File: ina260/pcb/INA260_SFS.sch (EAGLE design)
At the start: 52 parts

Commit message: finshed first design. after review ready for order
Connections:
- net SCL: now also BUS.P$1; no longer BUS.P$2
- net SDA: now also BUS.P$2; no longer BUS.P$1
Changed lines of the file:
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@@
 </busses>
 <nets>
-<net name="SCL" class="0">
-<segment>
-<pinref part="BUS" gate="J$1" pin="P$2"/>
-<wire x1="0" y1="8.89" x2="-10.16" y2="8.89" width="0.1524" layer="91"/>
-<label x="-10.16" y="6.35" size="1.778" layer="95"/>
-</segment>
-</net>
-<net name="SDA" class="0">
-<segment>
-<pinref part="BUS" gate="J$1" pin="P$1"/>
-<wire x1="0" y1="11.43" x2="-10.16" y2="11.43" width="0.1524" layer="91"/>
-<label x="-10.16" y="11.43" size="1.778" layer="95"/>
-</segment>
-</net>
 <net name="GND" class="0">
 <segment>
@@
 </segment>
 </net>
+<net name="SCL" class="0">
+<segment>
+<pinref part="BUS" gate="J$1" pin="P$1"/>
+<wire x1="0" y1="11.43" x2="-10.16" y2="11.43" width="0.1524" layer="91"/>
+<label x="-10.16" y="11.43" size="1.778" layer="95"/>
+</segment>
+</net>
+<net name="SDA" class="0">
+<segment>
+<pinref part="BUS" gate="J$1" pin="P$2"/>
+<wire x1="0" y1="8.89" x2="-10.16" y2="8.89" width="0.1524" layer="91"/>
+<label x="-10.16" y="6.35" size="1.778" layer="95"/>
+</segment>
+</net>

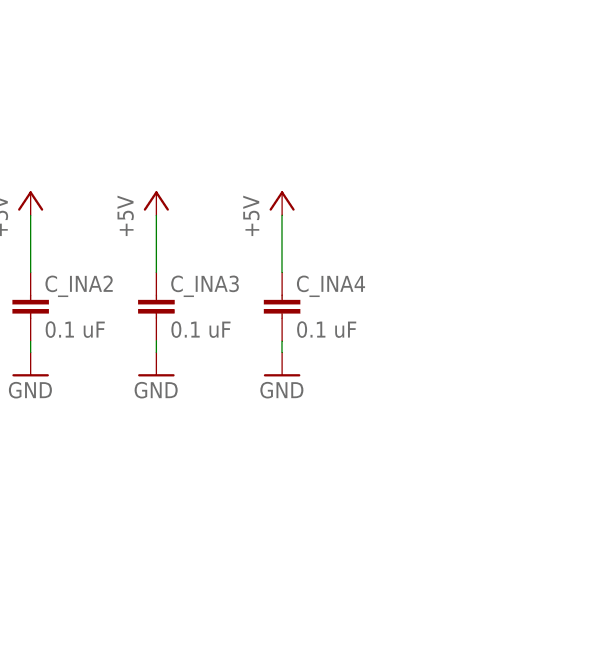
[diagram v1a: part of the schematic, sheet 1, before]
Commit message: added silkscreen layer pcb
logos added and descriptions of terminals 
also added i2c pullups and alive LED
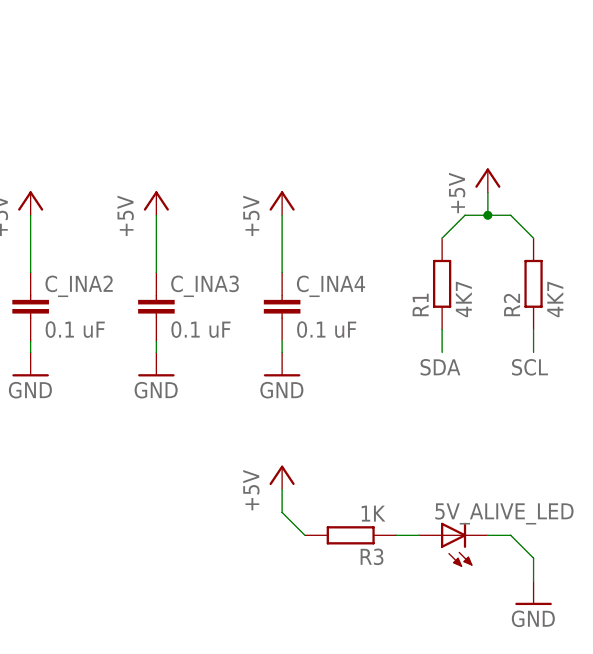
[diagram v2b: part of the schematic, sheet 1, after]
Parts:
- added 5V_ALIVE_LED: (no value), led:LEDSMT1206
- added R1, R2: 4K7, rcl:R-EU_M0805
- added R3: 1K, rcl:R-EU_M0805
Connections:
- new net N$2: 5V_ALIVE_LED.A, R3.1
- net +5V: now also R1.2, R2.2, R3.2
- net GND: now also 5V_ALIVE_LED.C
- net SCL: now also R2.1
- net SDA: now also R1.1
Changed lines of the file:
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@@
 <?xml version="1.0" encoding="utf-8"?>
 <!DOCTYPE eagle SYSTEM "eagle.dtd">
-<eagle version="9.4.2">
+<eagle version="9.5.0">
 <drawing>
 <settings>
@@
 <setting verticaltext="up"/>
 </settings>
-<grid distance="1.27" unitdist="mm" unit="mm" style="lines" multiple="1" display="no" altdistance="0.01" altunitdist="inch" altunit="mm"/>
+<grid distance="0.1" unitdist="inch" unit="inch" style="lines" multiple="1" display="no" altdistance="0.01" altunitdist="inch" altunit="inch"/>
 <layers>
 <layer number="1" name="Top" color="4" fill="1" visible="no" active="no"/>
@@
 <part name="GND23" library="supply1" library_urn="urn:adsk.eagle:library:371" deviceset="GND" device=""/>
 <part name="P+4" library="supply1" library_urn="urn:adsk.eagle:library:371" deviceset="+5V" device=""/>
+<part name="P+2" library="supply1" library_urn="urn:adsk.eagle:library:371" deviceset="+5V" device=""/>
+<part name="R1" library="rcl" library_urn="urn:adsk.eagle:library:334" deviceset="R-EU_" device="M0805" package3d_urn="urn:adsk.eagle:package:23556/2" value="4K7"/>
+<part name="R2" library="rcl" library_urn="urn:adsk.eagle:library:334" deviceset="R-EU_" device="M0805" package3d_urn="urn:adsk.eagle:package:23556/2" value="4K7"/>
+<part name="5V_ALIVE_LED" library="led" library_urn="urn:adsk.eagle:library:259" deviceset="LED" device="SMT1206" package3d_urn="urn:adsk.eagle:package:15796/1"/>
+<part name="R3" library="rcl" library_urn="urn:adsk.eagle:library:334" deviceset="R-EU_" device="M0805" package3d_urn="urn:adsk.eagle:package:23556/2" value="1K"/>
+<part name="P+7" library="supply1" library_urn="urn:adsk.eagle:library:371" deviceset="+5V" device=""/>
+<part name="GND24" library="supply1" library_urn="urn:adsk.eagle:library:371" deviceset="GND" device=""/>
 </parts>
 <sheets>
@@
 <attribute name="VALUE" x="30.48" y="-46.99" size="1.778" layer="96" rot="R90"/>
 </instance>
+<instance part="P+2" gate="1" x="40.64" y="-119.38" smashed="yes">
+<attribute name="VALUE" x="38.1" y="-124.46" size="1.778" layer="96" rot="R90"/>
+</instance>
+<instance part="R1" gate="G$1" x="35.56" y="-132.08" smashed="yes" rot="R90">
+<attribute name="NAME" x="34.0614" y="-135.89" size="1.778" layer="95" rot="R90"/>
+<attribute name="VALUE" x="38.862" y="-135.89" size="1.778" layer="96" rot="R90"/>
+</instance>
+<instance part="R2" gate="G$1" x="45.72" y="-132.08" smashed="yes" rot="R90">
+<attribute name="NAME" x="44.2214" y="-135.89" size="1.778" layer="95" rot="R90"/>
+<attribute name="VALUE" x="49.022" y="-135.89" size="1.778" layer="96" rot="R90"/>
+</instance>
+<instance part="5V_ALIVE_LED" gate="G$1" x="35.56" y="-160.02" smashed="yes" rot="R90">
+<attribute name="NAME" x="50.292" y="-156.464" size="1.778" layer="95" rot="R180"/>
+<attribute name="VALUE" x="40.132" y="-154.305" size="1.778" layer="96" rot="R180"/>
+</instance>
+<instance part="R3" gate="G$1" x="25.4" y="-160.02" smashed="yes" rot="R180">
+<attribute name="NAME" x="29.21" y="-161.5186" size="1.778" layer="95" rot="R180"/>
+<attribute name="VALUE" x="29.21" y="-156.718" size="1.778" layer="96" rot="R180"/>
+</instance>
+<instance part="P+7" gate="1" x="17.78" y="-152.4" smashed="yes">
+<attribute name="VALUE" x="15.24" y="-157.48" size="1.778" layer="96" rot="R90"/>
+</instance>
+<instance part="GND24" gate="1" x="45.72" y="-167.64" smashed="yes">
+<attribute name="VALUE" x="43.18" y="-170.18" size="1.778" layer="96"/>
+</instance>
 </instances>
 <busses>
@@
 <label x="20.32" y="-72.39" size="1.778" layer="95"/>
 </segment>
+<segment>
+<pinref part="R1" gate="G$1" pin="1"/>
+<wire x1="35.56" y1="-137.16" x2="35.56" y2="-139.7" width="0.1524" layer="91"/>
+<label x="33.02" y="-142.24" size="1.778" layer="95"/>
+</segment>
 </net>
 <net name="SCL" class="0">
@@
 <label x="20.32" y="-77.47" size="1.778" layer="95"/>
 <wire x1="45.72" y1="-77.47" x2="20.32" y2="-77.47" width="0.1524" layer="91"/>
+</segment>
+<segment>
+<pinref part="R2" gate="G$1" pin="1"/>
+<wire x1="45.72" y1="-137.16" x2="45.72" y2="-139.7" width="0.1524" layer="91"/>
+<label x="43.18" y="-142.24" size="1.778" layer="95"/>
 </segment>
 </net>
@@
 <wire x1="17.78" y1="-138.43" x2="17.78" y2="-139.7" width="0.1524" layer="91"/>
 <pinref part="GND16" gate="1" pin="GND"/>
+</segment>
+<segment>
+<pinref part="5V_ALIVE_LED" gate="G$1" pin="C"/>
+<wire x1="40.64" y1="-160.02" x2="43.18" y2="-160.02" width="0.1524" layer="91"/>
+<wire x1="43.18" y1="-160.02" x2="45.72" y2="-162.56" width="0.1524" layer="91"/>
+<wire x1="45.72" y1="-162.56" x2="45.72" y2="-165.1" width="0.1524" layer="91"/>
+<pinref part="GND24" gate="1" pin="GND"/>
 </segment>
 </net>
@@
 <wire x1="33.02" y1="-52.07" x2="33.02" y2="-44.45" width="0.1524" layer="91"/>
 </segment>
+<segment>
+<pinref part="R1" gate="G$1" pin="2"/>
+<wire x1="38.1" y1="-124.46" x2="35.56" y2="-127" width="0.1524" layer="91"/>
+<wire x1="38.1" y1="-124.46" x2="40.64" y2="-124.46" width="0.1524" layer="91"/>
+<pinref part="R2" gate="G$1" pin="2"/>
+<wire x1="40.64" y1="-124.46" x2="43.18" y2="-124.46" width="0.1524" layer="91"/>
+<wire x1="43.18" y1="-124.46" x2="45.72" y2="-127" width="0.1524" layer="91"/>
+<pinref part="P+2" gate="1" pin="+5V"/>
+<wire x1="40.64" y1="-124.46" x2="40.64" y2="-121.92" width="0.1524" layer="91"/>
+<junction x="40.64" y="-124.46"/>
+</segment>
+<segment>
+<pinref part="P+7" gate="1" pin="+5V"/>
+<wire x1="17.78" y1="-154.94" x2="17.78" y2="-157.48" width="0.1524" layer="91"/>
+<pinref part="R3" gate="G$1" pin="2"/>
+<wire x1="17.78" y1="-157.48" x2="20.32" y2="-160.02" width="0.1524" layer="91"/>
+</segment>
 </net>
 <net name="IN-_1" class="0">
@@
 <wire x1="-20.32" y1="-77.47" x2="-34.29" y2="-77.47" width="0.1524" layer="91"/>
 <label x="-34.29" y="-77.47" size="1.778" layer="95"/>
+</segment>
+</net>
+<net name="N$2" class="0">
+<segment>
+<pinref part="R3" gate="G$1" pin="1"/>
+<pinref part="5V_ALIVE_LED" gate="G$1" pin="A"/>
+<wire x1="30.48" y1="-160.02" x2="33.02" y2="-160.02" width="0.1524" layer="91"/>
 </segment>
 </net>
@@
 will not be understood (or retained) with this version.
 </note>
+<note version="8.3" severity="warning">
+Since Version 8.3, EAGLE supports the association of 3D packages
+with devices in libraries, schematics, and board files. Those 3D
+packages will not be understood (or retained) with this version.
+</note>
+<note version="8.4" severity="warning">
+Since Version 8.4, EAGLE supports properties for SPICE simulation.
+Probes in schematics and SPICE mapping objects found in parts and library devices
+will not be understood with this version. Update EAGLE to the latest version
+for full support of SPICE simulation.
+</note>
 </compatibility>

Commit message: 3.3 volt dc/dc converter
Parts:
- removed 5V: CON_3.81MM2_SIDE, Phoenix_connector_DJ:CON_3.81MM2_SIDE
- added C_INA5: 22 uF, Nordic_misc:CAPACITOR_0805_N
- added U$14: TSR1-2433, Traco power:TSR1-2433
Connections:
- net +5V: now also U$14.+3V3; no longer 5V.P$1
- net GND: now also C_INA5.2, U$14.GND; no longer 5V.P$2
- net IN+: now also C_INA5.1, U$14.IN
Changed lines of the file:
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@@
 <?xml version="1.0" encoding="utf-8"?>
 <!DOCTYPE eagle SYSTEM "eagle.dtd">
-<eagle version="9.5.0">
+<eagle version="9.4.2">
 <drawing>
 <settings>
@@
 <part name="GND21" library="supply1" library_urn="urn:adsk.eagle:library:371" deviceset="GND" device=""/>
 <part name="GND22" library="supply1" library_urn="urn:adsk.eagle:library:371" deviceset="GND" device=""/>
-<part name="5V" library="Phoenix_connector_DJ" deviceset="CON_3.81MM2_SIDE" device=""/>
-<part name="GND23" library="supply1" library_urn="urn:adsk.eagle:library:371" deviceset="GND" device=""/>
-<part name="P+4" library="supply1" library_urn="urn:adsk.eagle:library:371" deviceset="+5V" device=""/>
 <part name="P+2" library="supply1" library_urn="urn:adsk.eagle:library:371" deviceset="+5V" device=""/>
 <part name="R1" library="rcl" library_urn="urn:adsk.eagle:library:334" deviceset="R-EU_" device="M0805" package3d_urn="urn:adsk.eagle:package:23556/2" value="4K7"/>
@@
 <part name="P+7" library="supply1" library_urn="urn:adsk.eagle:library:371" deviceset="+5V" device=""/>
 <part name="GND24" library="supply1" library_urn="urn:adsk.eagle:library:371" deviceset="GND" device=""/>
+<part name="U$14" library="Traco power" deviceset="TSR1-2433" device=""/>
+<part name="C_INA5" library="Nordic_misc" deviceset="CAPACITOR" device="_0805_N" value="22 uF"/>
+<part name="GND25" library="supply1" library_urn="urn:adsk.eagle:library:371" deviceset="GND" device=""/>
+<part name="P+12" library="supply1" library_urn="urn:adsk.eagle:library:371" deviceset="+5V" device=""/>
 </parts>
 <sheets>
@@
 </instance>
 <instance part="P+2" gate="1" x="40.64" y="-119.38" smashed="yes">
-<attribute name="VALUE" x="38.1" y="-124.46" size="1.778" layer="96" rot="R90"/>
+<attribute name="VALUE" x="38.1" y="-119.38" size="1.778" layer="96" rot="R180"/>
 </instance>
 <instance part="R1" gate="G$1" x="35.56" y="-132.08" smashed="yes" rot="R90">
@@
 </instance>
 <instance part="P+7" gate="1" x="17.78" y="-152.4" smashed="yes">
-<attribute name="VALUE" x="15.24" y="-157.48" size="1.778" layer="96" rot="R90"/>
+<attribute name="VALUE" x="15.24" y="-152.4" size="1.778" layer="96" rot="R180"/>
 </instance>
 <instance part="GND24" gate="1" x="45.72" y="-167.64" smashed="yes">
@@
 <attribute name="VALUE" x="-8.89" y="21.59" size="1.778" layer="96"/>
 </instance>
-<instance part="5V" gate="J$1" x="0" y="-5.08" smashed="yes">
-<attribute name="NAME" x="0" y="0" size="1.778" layer="95"/>
-</instance>
-<instance part="GND23" gate="1" x="-6.35" y="-12.7" smashed="yes">
-<attribute name="VALUE" x="-8.89" y="-15.24" size="1.778" layer="96"/>
-</instance>
-<instance part="P+4" gate="1" x="-10.16" y="2.54" smashed="yes">
-<attribute name="VALUE" x="-12.7" y="-2.54" size="1.778" layer="96" rot="R90"/>
-</instance>
 </instances>
 <busses>
@@
 <junction x="-6.35" y="26.67"/>
 </segment>
-<segment>
-<pinref part="5V" gate="J$1" pin="P$2"/>
-<wire x1="0" y1="-5.08" x2="-6.35" y2="-5.08" width="0.1524" layer="91"/>
-<wire x1="-6.35" y1="-5.08" x2="-6.35" y2="-10.16" width="0.1524" layer="91"/>
-<pinref part="GND23" gate="1" pin="GND"/>
-</segment>
 </net>
 <net name="IN-_4" class="0">
@@
 </segment>
 </net>
-<net name="+5V" class="0">
-<segment>
-<pinref part="5V" gate="J$1" pin="P$1"/>
-<wire x1="0" y1="-2.54" x2="-10.16" y2="-2.54" width="0.1524" layer="91"/>
-<pinref part="P+4" gate="1" pin="+5V"/>
-<wire x1="-10.16" y1="0" x2="-10.16" y2="-2.54" width="0.1524" layer="91"/>
-</segment>
-</net>
 <net name="SCL" class="0">
 <segment>
@@
 </segment>
 </net>
+</nets>
+</sheet>
+<sheet>
+<plain>
+</plain>
+<instances>
+<instance part="U$14" gate="G$1" x="0" y="0" smashed="yes">
+<attribute name="NAME" x="-5.08" y="6.35" size="1.778" layer="95"/>
+<attribute name="VALUE" x="2.54" y="-7.62" size="1.778" layer="96"/>
+</instance>
+<instance part="C_INA5" gate="C$1" x="-17.78" y="-1.27" smashed="yes">
+<attribute name="NAME" x="-16.256" y="-0.889" size="1.778" layer="95"/>
+<attribute name="VALUE" x="-16.256" y="-5.969" size="1.778" layer="96"/>
+</instance>
+<instance part="GND25" gate="1" x="0" y="-12.7" smashed="yes">
+<attribute name="VALUE" x="-2.54" y="-15.24" size="1.778" layer="96"/>
+</instance>
+<instance part="P+12" gate="1" x="20.32" y="12.7" smashed="yes">
+<attribute name="VALUE" x="17.78" y="7.62" size="1.778" layer="96" rot="R90"/>
+</instance>
+</instances>
+<busses>
+</busses>
+<nets>
+<net name="IN+" class="0">
+<segment>
+<pinref part="U$14" gate="G$1" pin="IN"/>
+<wire x1="-10.16" y1="2.54" x2="-17.78" y2="2.54" width="0.1524" layer="91"/>
+<pinref part="C_INA5" gate="C$1" pin="1"/>
+<wire x1="-17.78" y1="2.54" x2="-30.48" y2="2.54" width="0.1524" layer="91"/>
+<wire x1="-17.78" y1="1.27" x2="-17.78" y2="2.54" width="0.1524" layer="91"/>
+<junction x="-17.78" y="2.54"/>
+<label x="-30.48" y="2.54" size="1.778" layer="95"/>
+</segment>
+</net>
+<net name="GND" class="0">
+<segment>
+<pinref part="C_INA5" gate="C$1" pin="2"/>
+<wire x1="-17.78" y1="-6.35" x2="-17.78" y2="-10.16" width="0.1524" layer="91"/>
+<wire x1="-17.78" y1="-10.16" x2="0" y2="-10.16" width="0.1524" layer="91"/>
+<pinref part="U$14" gate="G$1" pin="GND"/>
+<wire x1="0" y1="-10.16" x2="0" y2="-7.62" width="0.1524" layer="91"/>
+<pinref part="GND25" gate="1" pin="GND"/>
+<junction x="0" y="-10.16"/>
+</segment>
+</net>
+<net name="+5V" class="0">
+<segment>
+<pinref part="U$14" gate="G$1" pin="+3V3"/>
+<wire x1="10.16" y1="2.54" x2="20.32" y2="2.54" width="0.1524" layer="91"/>
+<wire x1="20.32" y1="2.54" x2="20.32" y2="10.16" width="0.1524" layer="91"/>
+<pinref part="P+12" gate="1" pin="+5V"/>
+</segment>
+</net>

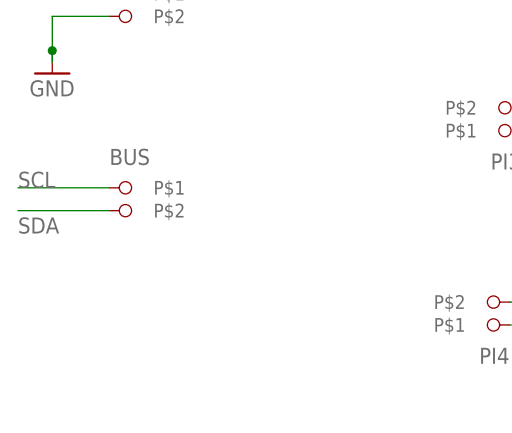
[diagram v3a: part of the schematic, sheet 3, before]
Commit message: added I2C second bus line terminal
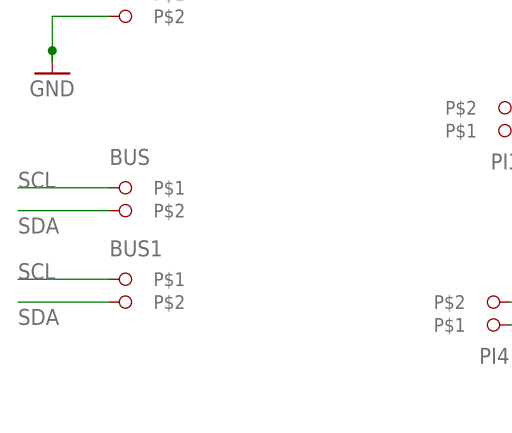
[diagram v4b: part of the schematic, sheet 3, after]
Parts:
- added BUS1: CON_3.81MM2_SIDE, Phoenix_connector_DJ:CON_3.81MM2_SIDE
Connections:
- net SCL: now also BUS1.P$1
- net SDA: now also BUS1.P$2
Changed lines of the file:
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@@
 <part name="GND25" library="supply1" library_urn="urn:adsk.eagle:library:371" deviceset="GND" device=""/>
 <part name="P+12" library="supply1" library_urn="urn:adsk.eagle:library:371" deviceset="+5V" device=""/>
+<part name="BUS1" library="Phoenix_connector_DJ" deviceset="CON_3.81MM2_SIDE" device=""/>
 </parts>
 <sheets>
@@
 <attribute name="VALUE" x="-8.89" y="21.59" size="1.778" layer="96"/>
 </instance>
+<instance part="BUS1" gate="J$1" x="0" y="-1.27" smashed="yes">
+<attribute name="NAME" x="0" y="3.81" size="1.778" layer="95"/>
+</instance>
 </instances>
 <busses>
@@
 <label x="-10.16" y="11.43" size="1.778" layer="95"/>
 </segment>
+<segment>
+<pinref part="BUS1" gate="J$1" pin="P$1"/>
+<wire x1="0" y1="1.27" x2="-10.16" y2="1.27" width="0.1524" layer="91"/>
+<label x="-10.16" y="1.27" size="1.778" layer="95"/>
+</segment>
 </net>
 <net name="SDA" class="0">
@@
 <label x="-10.16" y="6.35" size="1.778" layer="95"/>
 </segment>
-</net>
+<segment>
+<pinref part="BUS1" gate="J$1" pin="P$2"/>
+<wire x1="0" y1="-1.27" x2="-10.16" y2="-1.27" width="0.1524" layer="91"/>
+<label x="-10.16" y="-3.81" size="1.778" layer="95"/>
+</segment>
+</net>
